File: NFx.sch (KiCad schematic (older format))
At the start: 0 parts

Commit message: Push new .lib and .mod files to master
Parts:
- added CN1: MINIUSB, symbol MINIUSB
- added J?: PCIEPWR, PCIEPWR, symbol PCIEPWR
- added U1: MCP2210-SO, SSOP-20, symbol MCP2210-SO
- added U2: TXB0104, MODULE, symbol TXB0104
- added X1: QUARTZ-3P, symbol QUARTZ-3P
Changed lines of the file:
@@
-EESchema Schematic File Version 2
+EESchema Schematic File Version 2  date Thursday, February 20, 2014 'PMt' 01:48:51 PM
 LIBS:power
 LIBS:74xgxx
@@
 LIBS:video
 LIBS:xilinx
+LIBS:aat3220
+LIBS:aat3221igv
+LIBS:bd9c301fj
+LIBS:bitfury
+LIBS:capacitor-nonpolar
+LIBS:capacitor-polar
+LIBS:cp1
+LIBS:diode
+LIBS:ft232h
+LIBS:ft232rl
+LIBS:gnd-pwr
+LIBS:gnd
+LIBS:inductor-ironcore
+LIBS:inductor
+LIBS:led
+LIBS:mcp2210
+LIBS:miniusb
+LIBS:mos_n
+LIBS:ncp1117
+LIBS:quartz-3p
+LIBS:resistor
+LIBS:tst
+LIBS:vcc
+LIBS:TXB0104
+LIBS:con-molex-2
+LIBS:con-molex
+LIBS:k16
 LIBS:NFx-cache
-EELAYER 24 0
+EELAYER 27 0
 EELAYER END
 $Descr USLetter 11000 8500
 encoding utf-8
-Sheet 1 1
-Title ""
-Date ""
-Rev ""
+Sheet 1 3
+Title "NanoFury NFx"
+Date "20 feb 2014"
+Rev "43f0eac2"
 Comp ""
 Comment1 ""
@@
 Comment4 ""
 $EndDescr
+$Comp
+L MCP2210-SO U1
+U 1 1 530444C7
+P 3450 1400
+F 0 "U1" H 3950 1150 50  0000 L BNN
+F 1 "MCP2210-SO" H 3800 1300 50  0000 L BNN
+F 2 "SSOP-20" H 3800 1250 50  0001 L CNN
+F 3 "" H 4520 -575 60  0000 C CNN
+	1    3450 1400
+	1    0    0    -1
+$EndComp
+$Comp
+L MINIUSB CN1
+U 1 1 530454C9
+P 850 5500
+F 0 "CN1" H 900 5400 60  0000 C CNN
+F 1 "MINIUSB" H 940 5795 60  0000 C CNN
+F 2 "" H 950 5650 60  0000 C CNN
+F 3 "" H 950 5650 60  0000 C CNN
+	1    850  5500
+	-1   0    0    1
+$EndComp
+$Comp
+L TXB0104 U2
+U 1 1 53045865
+P 6150 2200
+F 0 "U2" H 6150 2100 50  0000 C CNN
+F 1 "TXB0104" H 6150 2300 50  0000 C CNN
+F 2 "MODULE" H 6150 2200 50  0001 C CNN
+F 3 "DOCUMENTATION" H 6150 2200 50  0001 C CNN
+	1    6150 2200
+	1    0    0    -1
+$EndComp
+$Comp
+L QUARTZ-3P X1
+U 1 1 530459E3
+P 1600 4100
+F 0 "X1" H 1600 4250 60  0000 C CNN
+F 1 "QUARTZ-3P" H 1600 4350 60  0000 C CNN
+F 2 "" H 1600 4100 60  0000 C CNN
+F 3 "" H 1600 4100 60  0000 C CNN
+	1    1600 4100
+	1    0    0    -1
+$EndComp
+$Comp
+L PCIEPWR J?
+U 1 1 530645D9
+P 800 6300
+F 0 "J?" H 850 5950 50  0000 L BNN
+F 1 "PCIEPWR" H 800 6400 50  0000 L BNN
+F 2 "PCIEPWR" H 950 6450 50  0001 C CNN
+F 3 "~" H 800 6300 60  0000 C CNN
+	1    800  6300
+	-1   0    0    1
+$EndComp
+$Sheet
+S 8000 5550 2400 1700
+U 530646F5
+F0 "Asic_Row_1" 50
+F1 "Asic_Row_1.sch" 50
+$EndSheet
+$Sheet
+S 5800 5550 2100 1700
+U 530649E0
+F0 "ASIC_Row_2" 50
+F1 "ASIC_Row_2.sch" 50
+$EndSheet
 $EndSCHEMATC

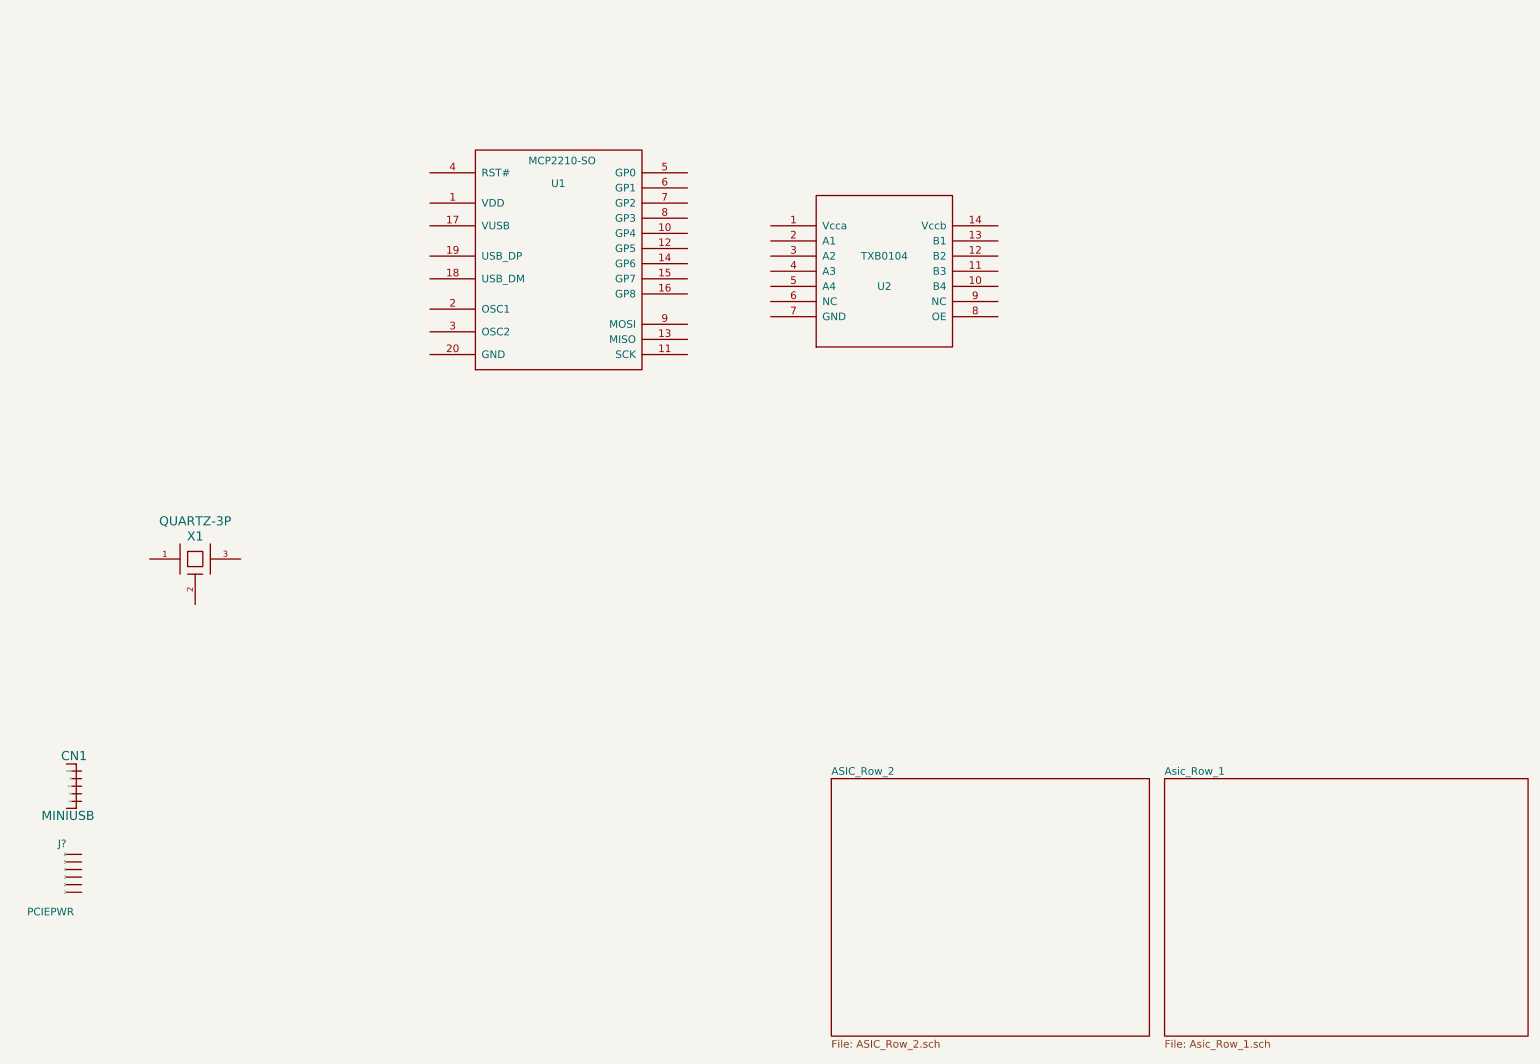
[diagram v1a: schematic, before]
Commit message: Finished schematic of VREG subsystem.
Moved from Rohm BD9C301 to TI TPS54327 to allow main power to be +12V
and lower min adjustable voltage to 0.76V
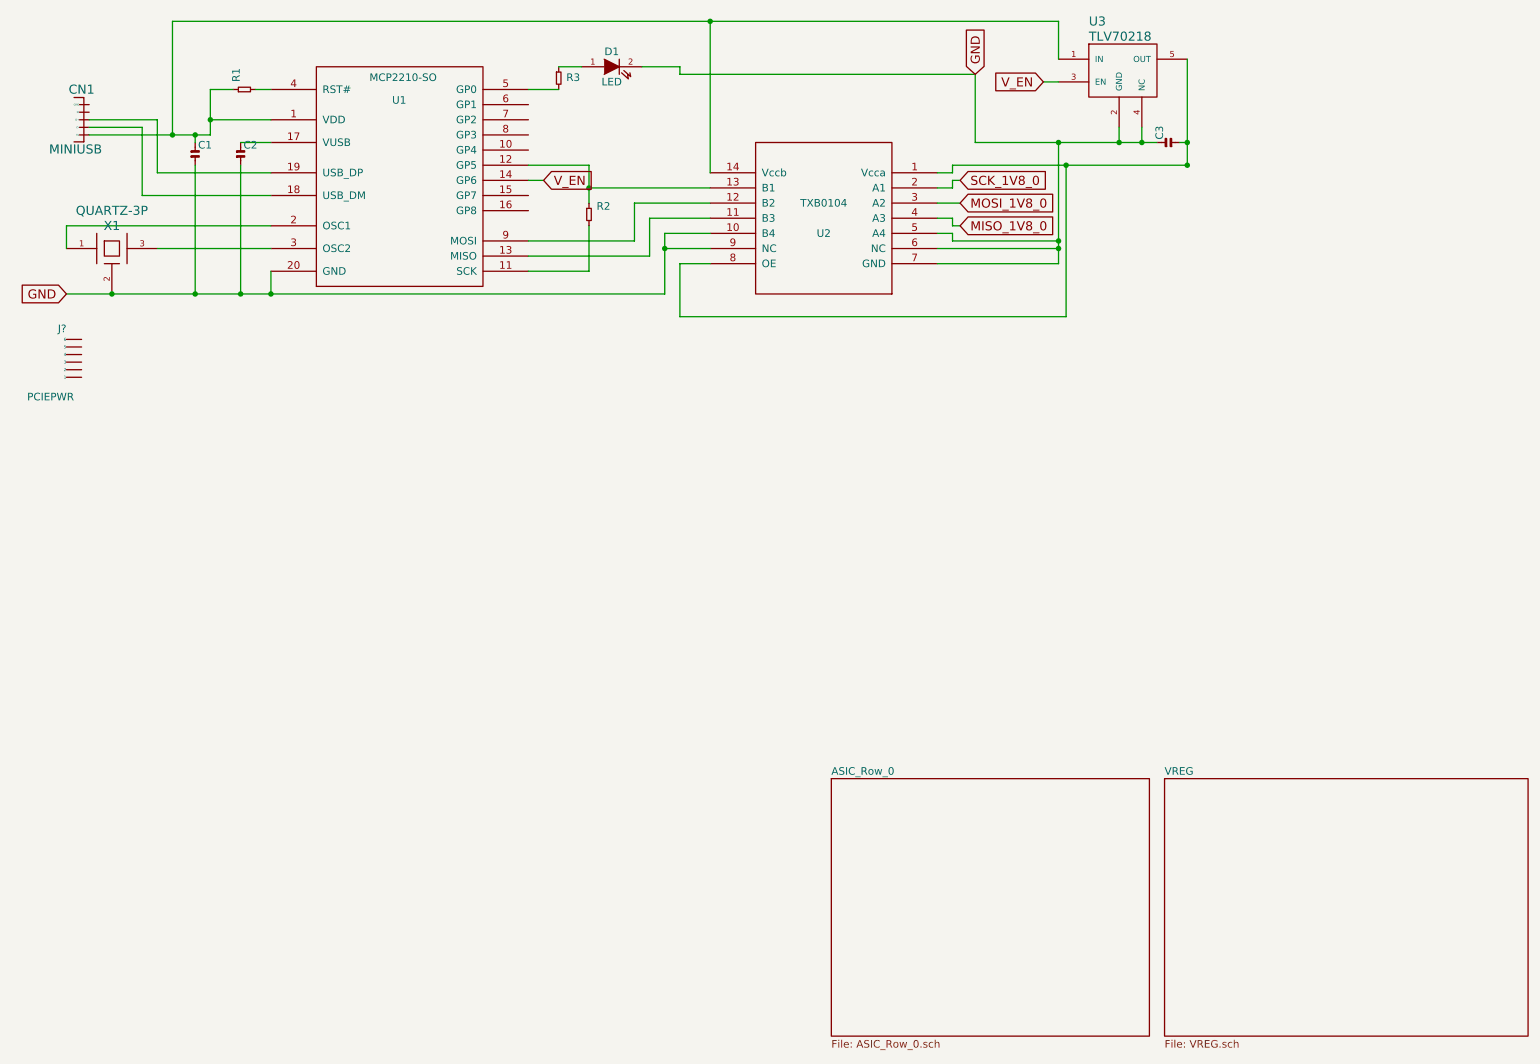
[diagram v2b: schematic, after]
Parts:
- added C1, C2, C3: CAPACITOR-NONPOLAR, symbol CAPACITOR-NONPOLAR
- added D1: LED, ~, symbol LED
- added R1, R2, R3: RESISTOR, symbol RESISTOR
- added U3: TLV70218, symbol AAT3221IGV
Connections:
- net at U1.1 (VDD): now also CN1.1 (5V), U2.14 (Vccb), C1.1, R1.2, U3.1 (IN)
- net at U1.11 (SCK): now also R2.1
- net at U1.12 (GP5): now also U2.13 (B1), R2.2
- net at U1.13 (MISO): now also U2.11 (B3)
- net V_EN: now reaches U1.14 (GP6)
- net V_EN: now also U3.3 (EN)
- net at U1.17 (VUSB): now also C2.1
- net at U1.18 (USB_DM): now also CN1.2 (D-)
- net at U1.19 (USB_DP): now also CN1.3 (D+)
- net at U1.2 (OSC1): now also X1.1
- net GND: now reaches U1.20 (GND)
- net GND: now also U2.10 (B4), U2.5 (A4), U2.6 (NC), U2.7 (GND), U2.9 (NC), X1.2 (GND), C1.2, C2.2, C3.1, D1.2 (K), U3.2 (GND), U3.4 (NC)
- net at U1.3 (OSC2): now also X1.3
- net at U1.4 (RST#): now also R1.1
- net at U1.5 (GP0): now also R3.1
- net at U1.9 (MOSI): now also U2.12 (B2)
- net at U2.1 (Vcca): now also U2.8 (OE), C3.2, U3.5 (OUT)
- net SCK_1V8_0: now reaches U2.2 (A1)
- net MOSI_1V8_0: now reaches U2.3 (A2)
- net MISO_1V8_0: now reaches U2.4 (A3)
- new net: D1.1 (A), R3.2
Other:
- moved on the sheet: CN1, J?, U1, U2, X1

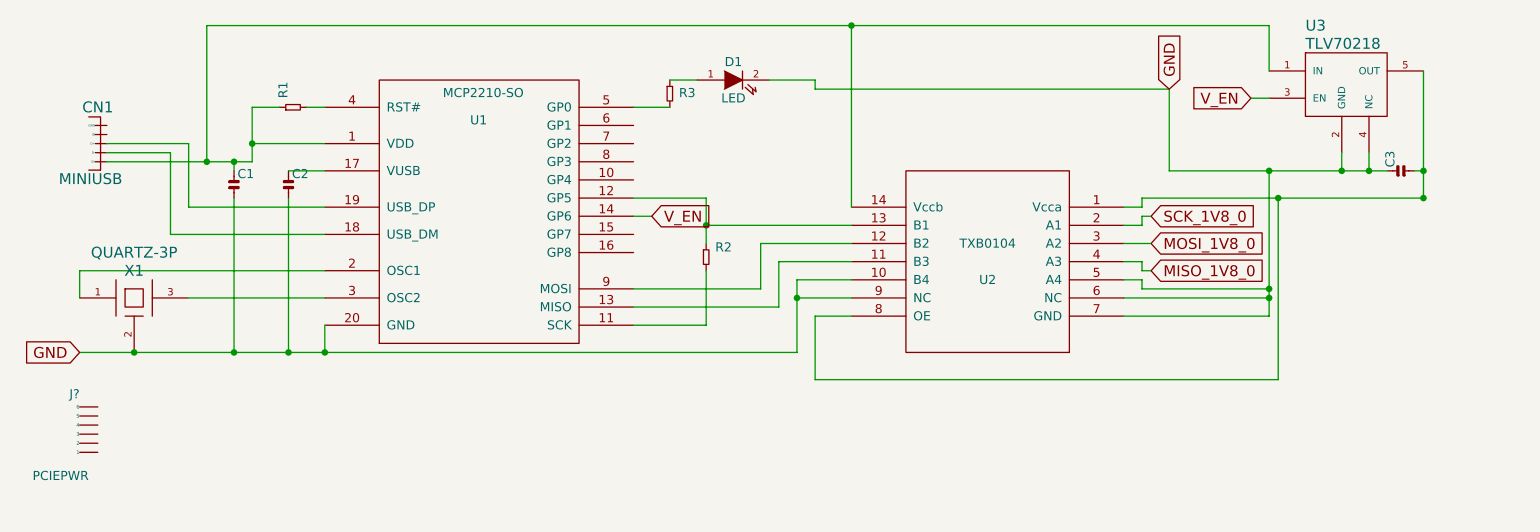
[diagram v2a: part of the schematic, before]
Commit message: Fill in component values in schematic
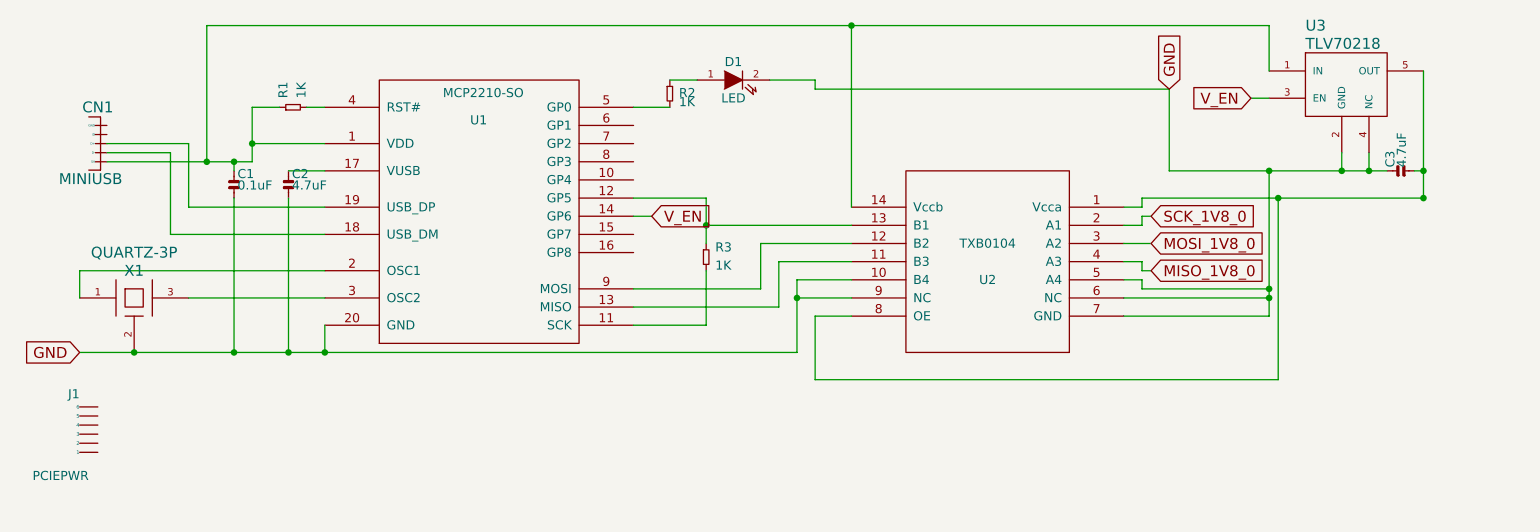
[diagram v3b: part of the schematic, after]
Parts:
- C1: value CAPACITOR-NONPOLAR -> 0.1uF
- C2, C3: value CAPACITOR-NONPOLAR -> 4.7uF
- R1: value RESISTOR -> 1K
- R2: renamed from R3; value RESISTOR -> 1K
- R3: renamed from R2; value RESISTOR -> 1K
- gave numbers to parts that had none: 1
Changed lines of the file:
@@
-EESchema Schematic File Version 2  date Friday, February 21, 2014 'AMt' 04:45:07 AM
+EESchema Schematic File Version 2  date Sunday, February 23, 2014 'AMt' 01:58:09 AM
 LIBS:power
 LIBS:74xgxx
@@
 Sheet 1 3
 Title "NanoFury NFx"
-Date "21 feb 2014"
+Date "23 feb 2014"
 Rev "43f0eac2"
 Comp ""
@@
 $EndComp
 $Comp
-L PCIEPWR J?
+L PCIEPWR J1
 U 1 1 530645D9
 P 800 2900
-F 0 "J?" H 850 2550 50  0000 L BNN
+F 0 "J1" H 850 2550 50  0000 L BNN
 F 1 "PCIEPWR" H 800 3000 50  0000 L BNN
 F 2 "PCIEPWR" H 950 3050 50  0001 C CNN
@@
 P 1850 1000
 F 0 "R1" H 1900 950 50  0000 L BNN
-F 1 "RESISTOR" H 1900 850 50  0001 L BNN
+F 1 "1K" H 1900 850 50  0000 L BNN
 F 2 "" H 1950 1100 50  0001 C CNN
 F 3 "" H 1755 1055 60  0000 C CNN
@@
 P 1600 1400
 F 0 "C1" H 1619 1404 50  0000 L BNN
-F 1 "CAPACITOR-NONPOLAR" H 1619 1341 50  0001 L BNN
+F 1 "0.1uF" H 1619 1341 50  0000 L BNN
 F 2 "" H 1600 1550 50  0001 C CNN
 F 3 "" H 1600 1400 60  0000 C CNN
@@
 P 1900 1400
 F 0 "C2" H 1919 1404 50  0000 L BNN
-F 1 "CAPACITOR-NONPOLAR" H 1919 1341 50  0001 L BNN
+F 1 "4.7uF" H 1919 1341 50  0000 L BNN
 F 2 "" H 1900 1550 50  0001 C CNN
 F 3 "" H 1900 1400 60  0000 C CNN
@@
 $EndComp
 $Comp
-L RESISTOR R2
+L RESISTOR R3
 U 1 1 5306E596
 P 4200 1750
-F 0 "R2" H 4250 1700 50  0000 L BNN
-F 1 "RESISTOR" H 4250 1600 50  0001 L BNN
+F 0 "R3" H 4250 1700 50  0000 L BNN
+F 1 "1K" H 4250 1600 50  0000 L BNN
 F 2 "" H 4300 1850 50  0001 C CNN
 F 3 "" H 4105 1805 60  0000 C CNN
@@
 Connection ~ 7300 2000
 $Comp
-L RESISTOR R3
+L RESISTOR R2
 U 1 1 5306EFDD
 P 4000 850
-F 0 "R3" H 4050 750 50  0000 L BNN
-F 1 "RESISTOR" H 4050 700 50  0001 L BNN
+F 0 "R2" H 4050 750 50  0000 L BNN
+F 1 "1K" H 4050 700 50  0000 L BNN
 F 2 "" H 4100 950 50  0001 C CNN
 F 3 "" H 3905 905 60  0000 C CNN
@@
 P 8000 1350
 F 0 "C3" H 8019 1354 50  0000 L BNN
-F 1 "CAPACITOR-NONPOLAR" H 8019 1291 50  0001 L BNN
+F 1 "4.7uF" H 8019 1291 50  0000 L BNN
 F 2 "" H 8000 1500 50  0001 C CNN
 F 3 "" H 8000 1350 60  0000 C CNN

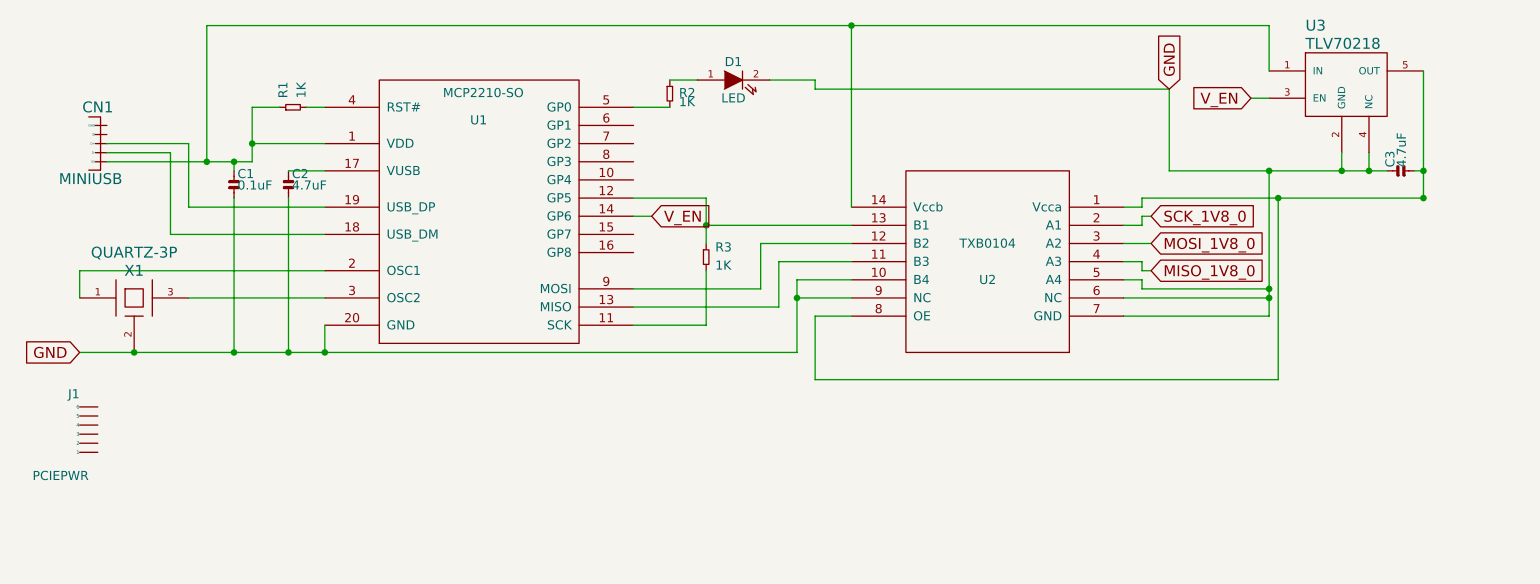
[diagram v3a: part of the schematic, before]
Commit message: Added ASIC row 0 and added links for power domains and comm lines
Renumbered components.

Added LED on MCP2210 GP3 pin to show SPI traffic activity (this feature
will require either programming of the NFx to modify NVRAM boot
settings [most likely], or added driver code in mcp init block [less
likely])
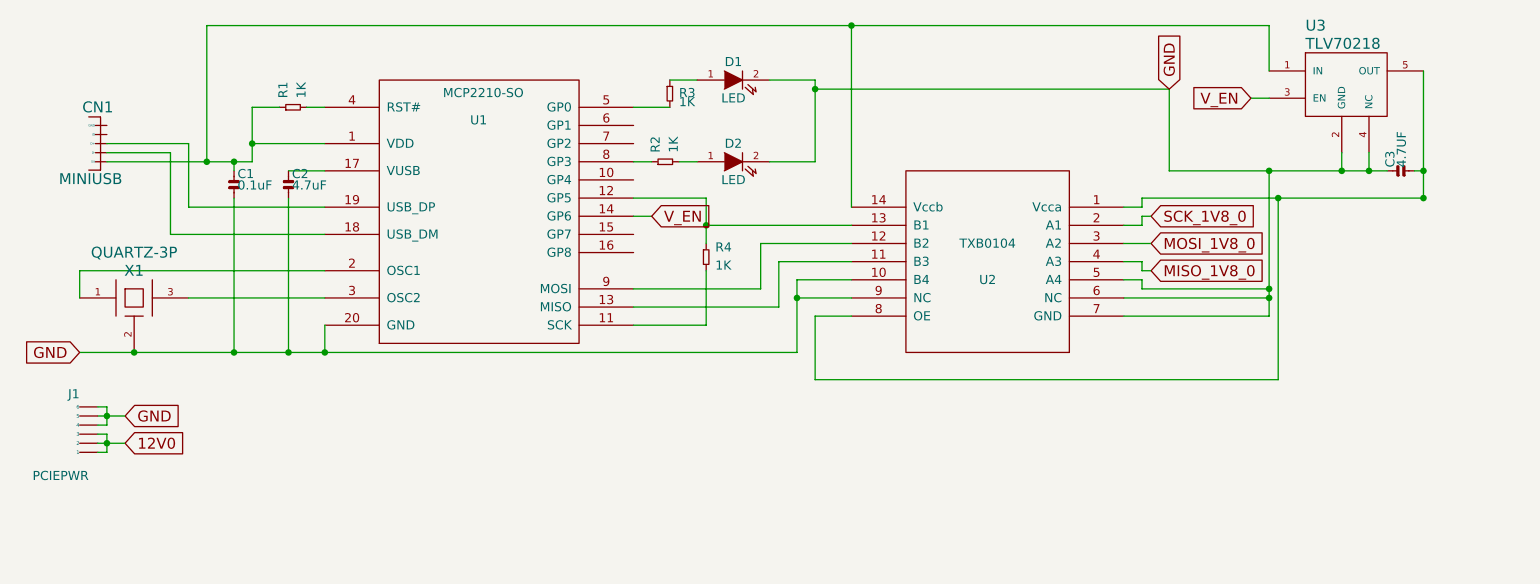
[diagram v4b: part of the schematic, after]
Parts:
- added D2: LED, ~, symbol LED
- added R2: 1K, symbol RESISTOR
- C3: value 4.7uF -> 4.7UF
- renumbered R2 to R3, R3 to R4
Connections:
- net GND: now also J1.4, J1.5, J1.6, D2.2 (K)
- net at U1.8 (GP3): now also R2.2
- net 12V0: now reaches J1.1
- net 12V0: now also J1.2, J1.3
- new net: D2.1 (A), R2.1
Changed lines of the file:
@@
-EESchema Schematic File Version 2  date Sunday, February 23, 2014 'AMt' 01:58:09 AM
+EESchema Schematic File Version 2  date Monday, February 24, 2014 'AMt' 12:37:09 AM
 LIBS:power
 LIBS:74xgxx
@@
 Sheet 1 3
 Title "NanoFury NFx"
-Date "23 feb 2014"
+Date "24 feb 2014"
 Rev "43f0eac2"
 Comp ""
@@
 $EndComp
 $Comp
-L RESISTOR R3
+L RESISTOR R4
 U 1 1 5306E596
 P 4200 1750
-F 0 "R3" H 4250 1700 50  0000 L BNN
+F 0 "R4" H 4250 1700 50  0000 L BNN
 F 1 "1K" H 4250 1600 50  0000 L BNN
 F 2 "" H 4300 1850 50  0001 C CNN
@@
 Connection ~ 7300 2000
 $Comp
-L RESISTOR R2
+L RESISTOR R3
 U 1 1 5306EFDD
 P 4000 850
-F 0 "R2" H 4050 750 50  0000 L BNN
+F 0 "R3" H 4050 750 50  0000 L BNN
 F 1 "1K" H 4050 700 50  0000 L BNN
 F 2 "" H 4100 950 50  0001 C CNN
@@
 	4550 850  4800 850
 Wire Wire Line
-	4800 850  4800 900
-Wire Wire Line
-	4800 900  6750 900
+	4800 850  4800 1300
+Wire Wire Line
+	6750 900  4800 900
 $Comp
 L CAPACITOR-NONPOLAR C3
@@
 P 8000 1350
 F 0 "C3" H 8019 1354 50  0000 L BNN
-F 1 "4.7uF" H 8019 1291 50  0000 L BNN
+F 1 "4.7UF" H 8019 1291 50  0000 L BNN
 F 2 "" H 8000 1500 50  0001 C CNN
 F 3 "" H 8000 1350 60  0000 C CNN
@@
 	8100 1350 8150 1350
 Connection ~ 8150 1350
+Text GLabel 1000 2850 2    60   Input ~ 0
+12V0
+Text GLabel 1000 2700 2    60   Input ~ 0
+GND
+Wire Wire Line
+	850  2850 1000 2850
+Wire Wire Line
+	850  2700 1000 2700
+Wire Wire Line
+	850  2650 900  2650
+Wire Wire Line
+	900  2650 900  2750
+Connection ~ 900  2700
+Wire Wire Line
+	900  2750 850  2750
+Wire Wire Line
+	850  2800 900  2800
+Wire Wire Line
+	900  2800 900  2900
+Connection ~ 900  2850
+Wire Wire Line
+	900  2900 850  2900
+$Comp
+L LED D2
+U 1 1 530AD565
+P 4350 1300
+F 0 "D2" H 4350 1400 50  0000 C CNN
+F 1 "LED" H 4350 1200 50  0000 C CNN
+F 2 "~" H 4350 1300 60  0000 C CNN
+F 3 "~" H 4350 1300 60  0000 C CNN
+	1    4350 1300
+	1    0    0    -1
+$EndComp
+$Comp
+L RESISTOR R2
+U 1 1 530AD574
+P 3900 1300
+F 0 "R2" H 3950 1250 50  0000 L BNN
+F 1 "1K" H 3950 1150 50  0000 L BNN
+F 2 "" H 4000 1400 50  0001 C CNN
+F 3 "" H 3805 1355 60  0000 C CNN
+	1    3900 1300
+	0    -1   -1   0
+$EndComp
+Wire Wire Line
+	3800 1300 3900 1300
+Wire Wire Line
+	4050 1300 4150 1300
+Wire Wire Line
+	4800 1300 4550 1300
+Connection ~ 4800 900
 $EndSCHEMATC
